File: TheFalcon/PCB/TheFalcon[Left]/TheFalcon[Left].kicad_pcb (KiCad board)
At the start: 2 copper layers, 173.3 x 142.5 mm, 171 parts, among them IC1 IS31FL3729-QFLS4-TR, J2 Conn_01x04_Pin, J3 Conn_01x04_Pin, J5 Conn_01x01, J6 Conn_01x01, SW1 SW_Push, SW2 SW_Push, U2 USBLC6-2P6, U3 USBLC6-2P6, U4 AMS1117-3.3, U6 STM32G431CBTx, Y1 X322516MOB4SI

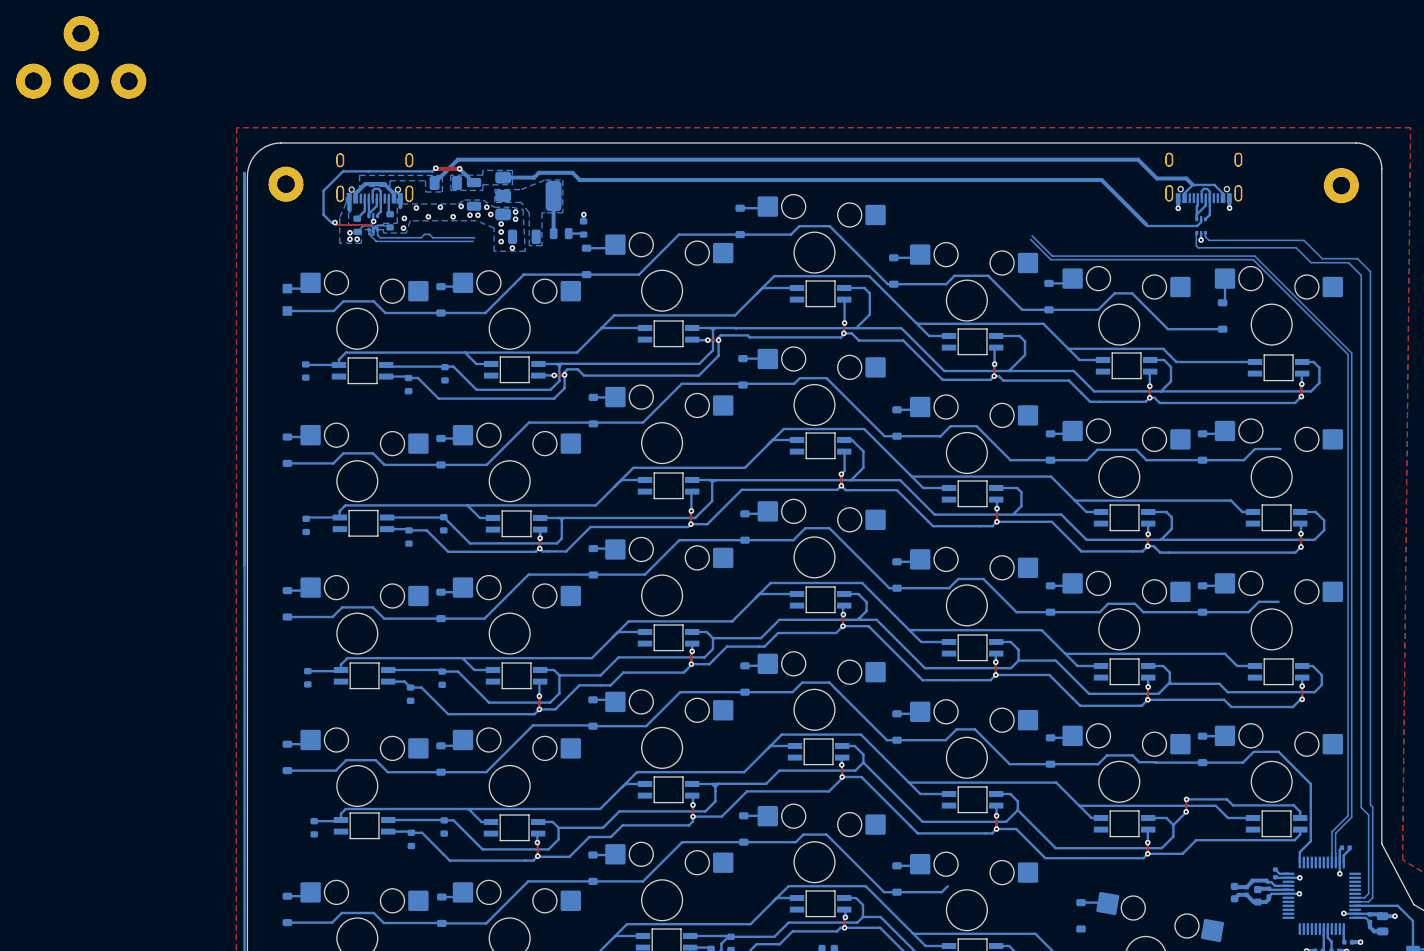
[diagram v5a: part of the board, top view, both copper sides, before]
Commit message: TwoUSBs on Top
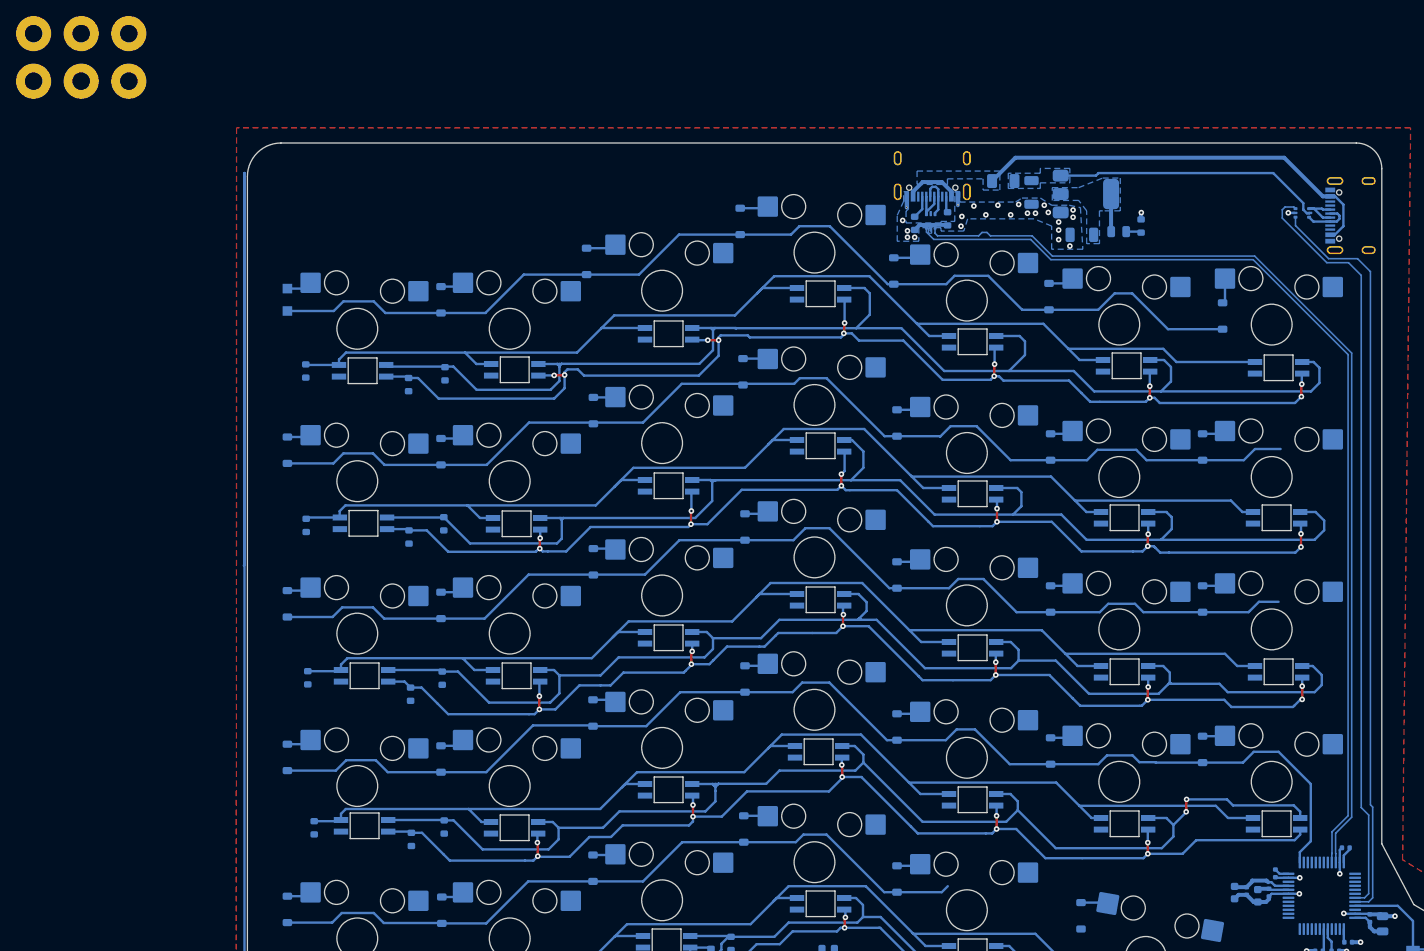
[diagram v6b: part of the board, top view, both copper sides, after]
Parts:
- moved H5 164.6 mm to (-7.12, 10.7)
- moved C10 69.7 mm to (117.6, 30.6)
- moved C11 69.7 mm to (123.9, 35.9)
- moved F1 69.7 mm to (114.1, 29.2)
- moved R1 69.7 mm to (103.0, 34.4)
- moved R2 69.7 mm to (107.1, 33.9)
- moved R25 69.7 mm to (131.3, 34.8)
- moved U2 69.7 mm to (105.0, 34.1)
- moved U4 69.7 mm to (124.4, 30.8)
- moved USB1 69.7 mm to (105.2, 27.4)
- moved D39 69.7 mm to (128.5, 35.5)
- moved H1 27.2 mm to (4.78, 10.7)
- moved USB2 20.4 mm to (158.7, 33.5), turned to -90 degrees
- moved U3 12.7 mm to (151.5, 33.1), turned to 0 degrees
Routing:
- net +5V: track 125.3 -> 36.7 mm, vias 4 -> 0
- net VBUS: track 111.2 -> 59.4 mm
- net USB_Tx-: track 103.7 -> 93.6 mm
- net USB_Tx+: track 103.4 -> 95.3 mm
- net GND: track 51.4 -> 50.9 mm, vias 36 -> 35

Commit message: Save
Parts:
- moved H2 47.1 mm to (48.2, 35.0)
- moved H3 47.1 mm to (42.2, 29.1)
- moved H4 47.1 mm to (42.2, 35.0)
- moved H5 47.1 mm to (36.3, 29.1)
- moved H6 47.1 mm to (36.3, 35.0)
- moved H1 28.5 mm to (26.0, 29.8)
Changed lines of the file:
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@@
 	(footprint "MountingHole:MountingHole_2.2mm_M2_Pad"
 		(layer "B.Cu")
-		(at 4.775 16.675 180)
+		(at 48.2 35 180)
 		(descr "Mounting Hole 2.2mm, M2, generated by kicad-footprint-generator mountinghole.py")
 		(tags "mountinghole M2")
@@
 	(footprint "MountingHole:MountingHole_2.2mm_M2_Pad"
 		(layer "B.Cu")
-		(at -7.125 16.675 180)
+		(at 36.3 35 180)
 		(descr "Mounting Hole 2.2mm, M2, generated by kicad-footprint-generator mountinghole.py")
 		(tags "mountinghole M2")
@@
 	(footprint "MountingHole:MountingHole_2.2mm_M2_Pad"
 		(layer "B.Cu")
-		(at -7.125 10.725 180)
+		(at 36.3 29.05 180)
 		(descr "Mounting Hole 2.2mm, M2, generated by kicad-footprint-generator mountinghole.py")
 		(tags "mountinghole M2")
@@
 	(footprint "MountingHole:MountingHole_2.2mm_M2_Pad"
 		(layer "B.Cu")
-		(at -1.175 16.675 180)
+		(at 42.25 35 180)
 		(descr "Mounting Hole 2.2mm, M2, generated by kicad-footprint-generator mountinghole.py")
 		(tags "mountinghole M2")
@@
 	(footprint "MountingHole:MountingHole_2.2mm_M2_Pad"
 		(layer "B.Cu")
-		(at 4.775 10.725 180)
+		(at 26 29.8 180)
 		(descr "Mounting Hole 2.2mm, M2, generated by kicad-footprint-generator mountinghole.py")
 		(tags "mountinghole M2")
@@
 	(footprint "MountingHole:MountingHole_2.2mm_M2_Pad"
 		(layer "B.Cu")
-		(at -1.175 10.725 180)
+		(at 42.25 29.05 180)
 		(descr "Mounting Hole 2.2mm, M2, generated by kicad-footprint-generator mountinghole.py")
 		(tags "mountinghole M2")

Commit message: Save
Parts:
- moved C12 114.7 mm to (28.5, 31.2)
- moved IC1 114.7 mm to (26.9, 34.4)
- moved R24 114.7 mm to (35.0, 34.7)
- moved C13 114.7 mm to (28.5, 29.7)
- moved R33 114.7 mm to (35.0, 31.7)
- moved R6 114.7 mm to (30.5, 31.9)
- moved C14 105.0 mm to (57.1, 37.1)
- moved R5 105.0 mm to (58.4, 37.0)
- moved H2 61.4 mm to (-7.40, 9.00)
- moved H4 61.4 mm to (-13.3, 9.00)
- moved H6 61.4 mm to (-19.3, 9.00)
- moved H1 55.5 mm to (-21.4, 0.95)
- moved H3 55.5 mm to (-5.20, 0.20)
- moved H5 55.5 mm to (-11.2, 0.20)
- moved R9 13.5 mm to (40.0, 49.6), turned to 90 degrees
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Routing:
- net (no net): track 154.8 -> 0.00 mm
- net +5V: track 36.7 -> 141.1 mm, vias 0 -> 2
- net /RGB Array/CS1: track 0.00 -> 19.0 mm, vias 0 -> 2
- net /RGB Array/B_RGB_ROW_0: track 152.4 -> 148.2 mm
- net GND: track 50.9 -> 52.1 mm, vias 35 -> 40
- net VBUS: track 59.4 -> 60.5 mm
- net USB_MCU_D+: track 123.7 -> 123.0 mm
